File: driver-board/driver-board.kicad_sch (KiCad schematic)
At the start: 54 parts, among them J1 MCP4725, J2 Conn_Coaxial, J3 MCP4725, J4 Conn_Coaxial, SW1 RST, SW2 BIAS ON/OF, U1 Pico, U2 MIC5317, U3 TSV358, U4 TSV358, U5 TCBT-2R5G, U6 LM2904, U7 LT3462A

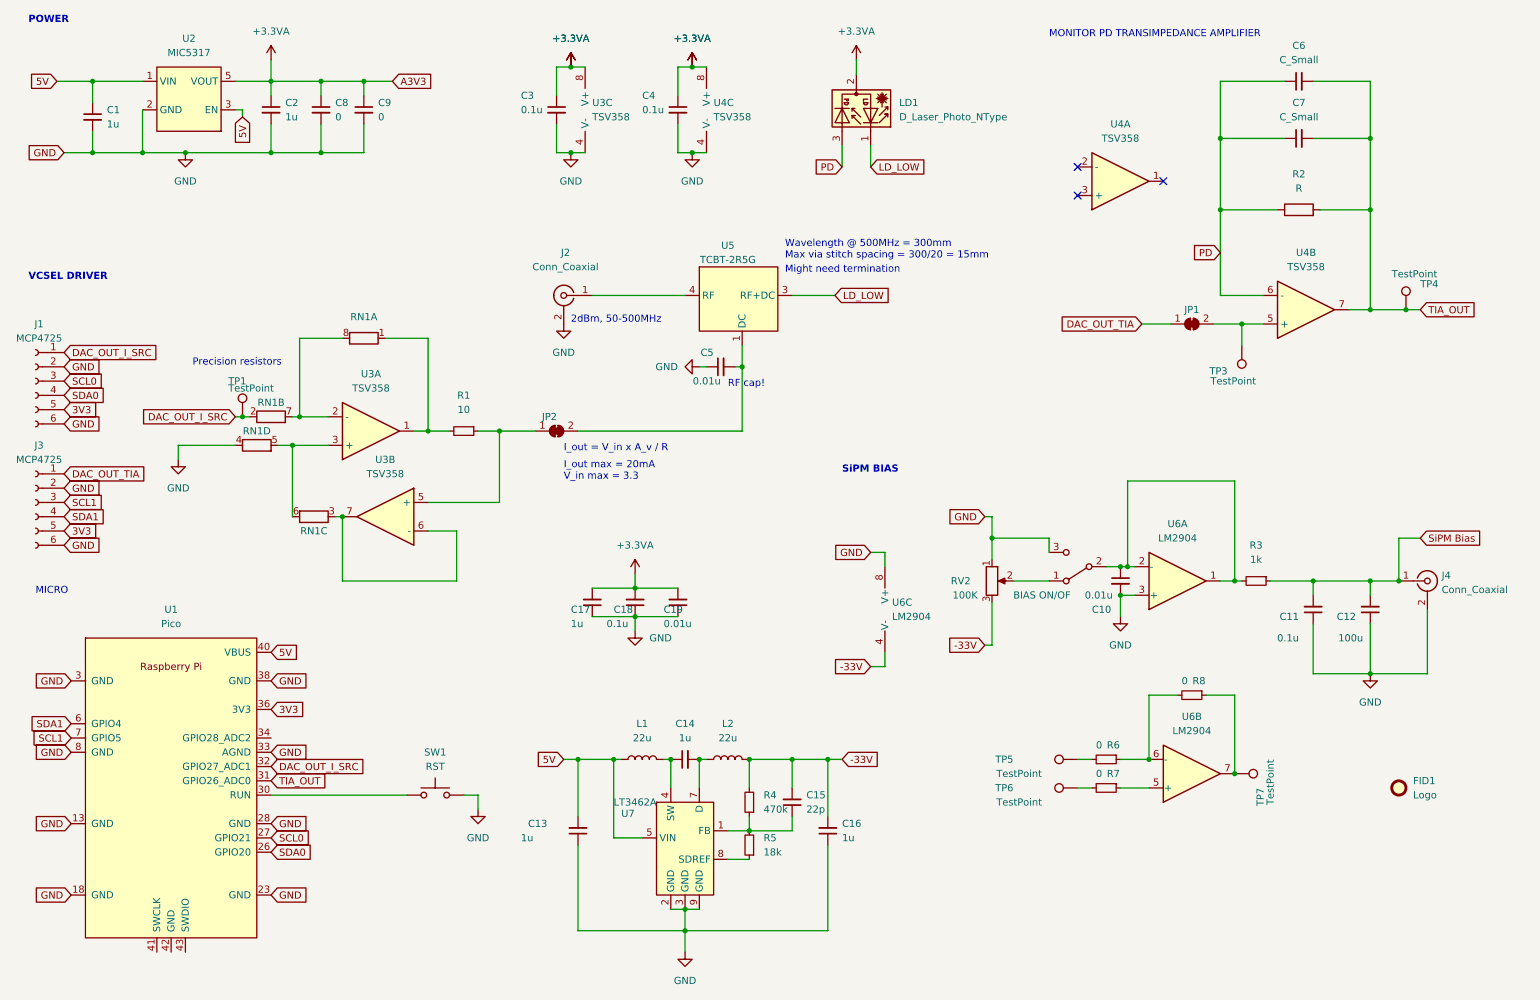
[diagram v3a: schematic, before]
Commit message: Cleanup, trying simpler board with no RF switch
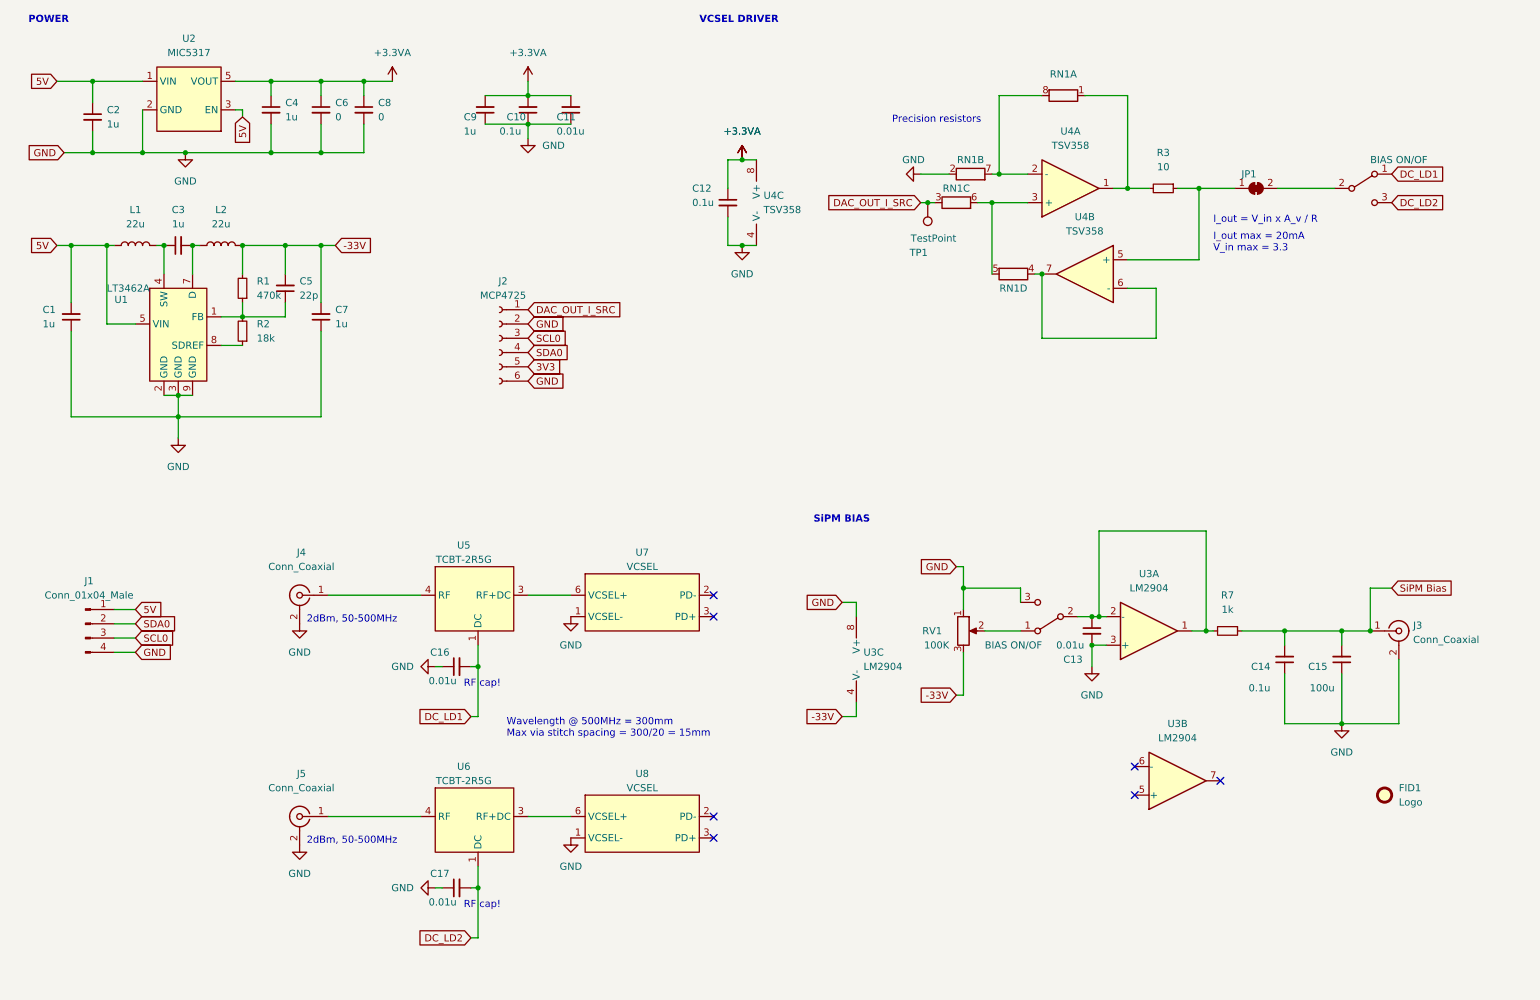
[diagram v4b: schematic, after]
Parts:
- removed C4: 0.1u, Capacitor_SMD:C_0805_2012Metric_Pad1.18x1.45mm_HandSolder, symbol Device:C_Small
- removed C6, C7: C_Small, Capacitor_SMD:C_0805_2012Metric_Pad1.18x1.45mm_HandSolder, symbol Device:C_Small
- removed J3: MCP4725, Connector_PinSocket_2.54mm:PinSocket_1x06_P2.54mm_Vertical, symbol Connector:Conn_01x06_Female
- removed JP1: SolderJumper_2_Open, Jumper:SolderJumper-2_P1.3mm_Bridged_Pad1.0x1.5mm, symbol Jumper:SolderJumper_2_Bridged
- removed LD1: D_Laser_Photo_NType, Package_TO_SOT_THT:TO-46-3, symbol Device:D_Laser_Photo_NType
- removed R2: R, Resistor_SMD:R_0805_2012Metric_Pad1.20x1.40mm_HandSolder, symbol Device:R
- removed R6, R7, R8: 0, Resistor_SMD:R_0805_2012Metric_Pad1.20x1.40mm_HandSolder, symbol Device:R_Small
- removed SW1: RST, lib:PTS636 SM43J, symbol Switch:SW_Push
- removed TP3, TP4, TP5, TP6, TP7: TestPoint, TestPoint:TestPoint_Pad_D1.5mm, symbol Connector:TestPoint
- removed U1: Pico, lib:RPi_Pico_minimal, symbol fd-fnir:Pico_minimal
- removed U4: TSV358, lib:SOIC-8-1EP_3.9x4.9mm_P1.27mm_EP2.29x3mm, symbol fd-fnir:TSV358
- added C17: 0.01u, Capacitor_SMD:C_0805_2012Metric_Pad1.18x1.45mm_HandSolder, symbol Device:C_Small
- added J1: Conn_01x04_Male, Connector_PinHeader_2.54mm:PinHeader_1x04_P2.54mm_Vertical, symbol Connector:Conn_01x04_Male
- added J5: Conn_Coaxial, lib:CONSMA020.062-G, symbol Connector:Conn_Coaxial
- added SW2: BIAS ON/OF, lib:JS202011SCQN, symbol Switch:SW_DPDT_x2
- added U6: TCBT-2R5G, lib:TCBT, symbol fd-fnir:TCBT-2R5G
- added U7, U8: VCSEL, lib:VP-SMD-5050, symbol fd-fnir:VCSEL
- renumbered C13 to C1, C18 to C10, C19 to C11, C3 to C12, C10 to C13, C11 to C14, C12 to C15, C5 to C16, C1 to C2, C14 to C3, C2 to C4, C15 to C5, C8 to C6, C16 to C7, C9 to C8, C17 to C9, J1 to J2, J4 to J3, J2 to J4, JP2 to JP1, R4 to R1, R5 to R2, R1 to R3, R3 to R7, RV2 to RV1, SW2 to SW1, U7 to U1, U6 to U3, U3 to U4
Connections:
- net 5V: now also J1.1 (Pin_1)
- net DAC_OUT_I_SRC: now also RN1.3 (R3.1); no longer RN1.2 (R2.1)
- net GND: now also RN1.2 (R2.1), C17.1, J1.4 (Pin_4), J5.2 (Ext), U7.1 (VCSEL-), U8.1 (VCSEL-); no longer RN1.4 (R4.1)
- net SCL0: now also J1.3 (Pin_3)
- net SDA0: now also J1.2 (Pin_2)
- net DC_LD1: now reaches C16.2, U5.1 (DC)
- net DC_LD1: now also SW2.1 (A); no longer JP1.2 (B)
- net at U4.6 (-), U4.7: now also RN1.4 (R4.1); no longer RN1.3 (R3.1)
- net LD_LOW: no longer names the net of U5.3 (RF+DC)
- net LD_LOW: now also U7.6 (VCSEL+)
- new net: JP1.2 (B), SW2.2 (B)
- new net: U6.3 (RF+DC), U8.6 (VCSEL+)
- new net: J5.1 (In), U6.4 (RF)
- new net DC_LD2: C17.2, SW2.3 (C), U6.1 (DC)
- no-connect marks 3 -> 7
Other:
- note removed: "MICRO"
- note removed: "MONITOR PD TRANSIMPEDANCE AMPLIFIER"
- note removed: "Might need termination"
- moved on the sheet: C1, C10, C11, C12, C13, C14, C15, C16, C3, C5, C7, C9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
